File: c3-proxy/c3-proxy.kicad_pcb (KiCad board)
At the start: 4 copper layers, 69.8 x 50 mm, 73 parts, among them J1 TFM-120-X1-XXX-D-RA, J2 SFM-120-02-L-DH, J3 USB_C_Receptacle_USB2.0_16P, J4 Barrel_Jack_Switch_MountingPin, J5 Conn_01x04, Q2 DMP2035UQ-7, Q5 DMP2035UQ-7, Q6 31-DMN2053UQ-13CT-ND, Q7 DMP2035UQ-7, Q8 DMP2035UQ-7, SW1 C&K PCM13SMTR, SW2 SW_DP3T, U1 MCP2221AxST, U2 INA226, U3 LTC4412xS6, U4 LTC4412xS6, U5 TS5A21366, U6 MAX892LEUA+T, U7 MIC23050-SYML, U8 LTC4412xS6, U9 IP4234CZ6,125

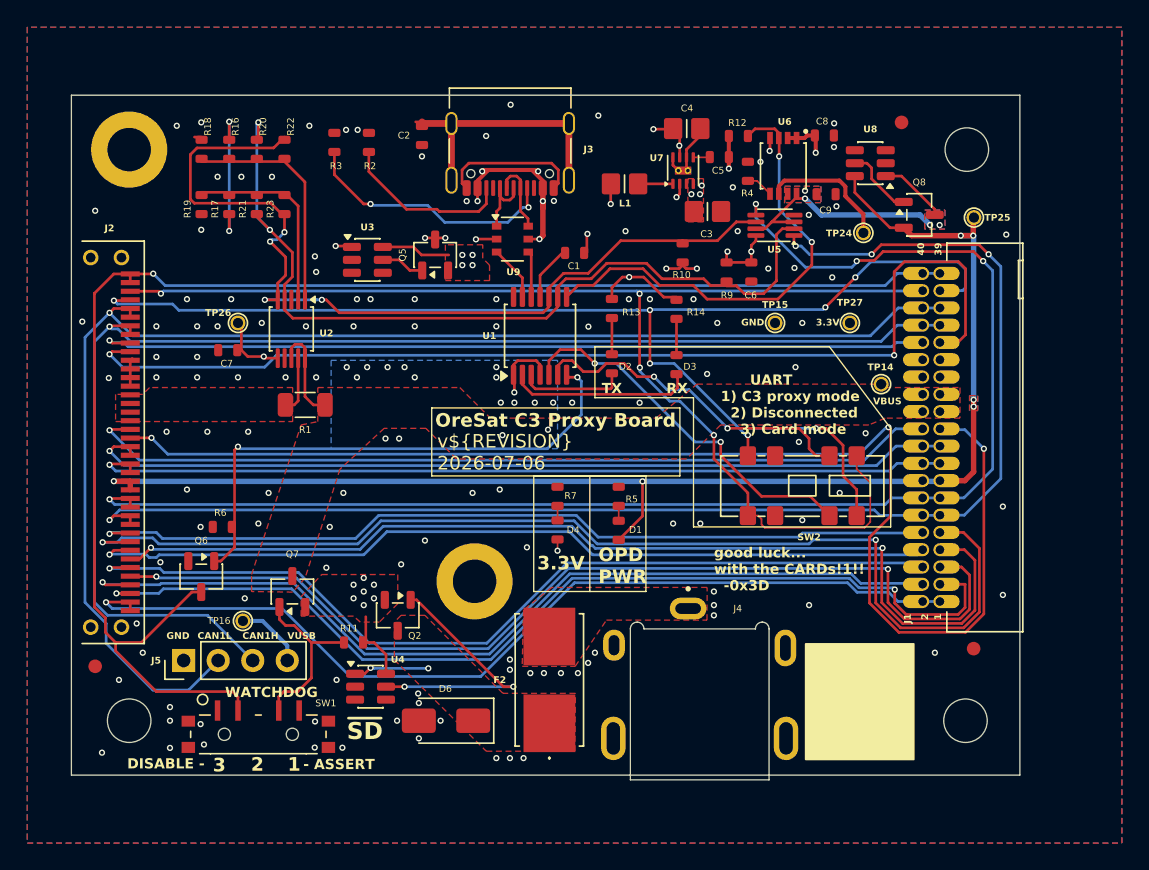
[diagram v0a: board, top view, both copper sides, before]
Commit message: changed footprints in schematic
so that "update from schematic" doesn't kill my baby resistors
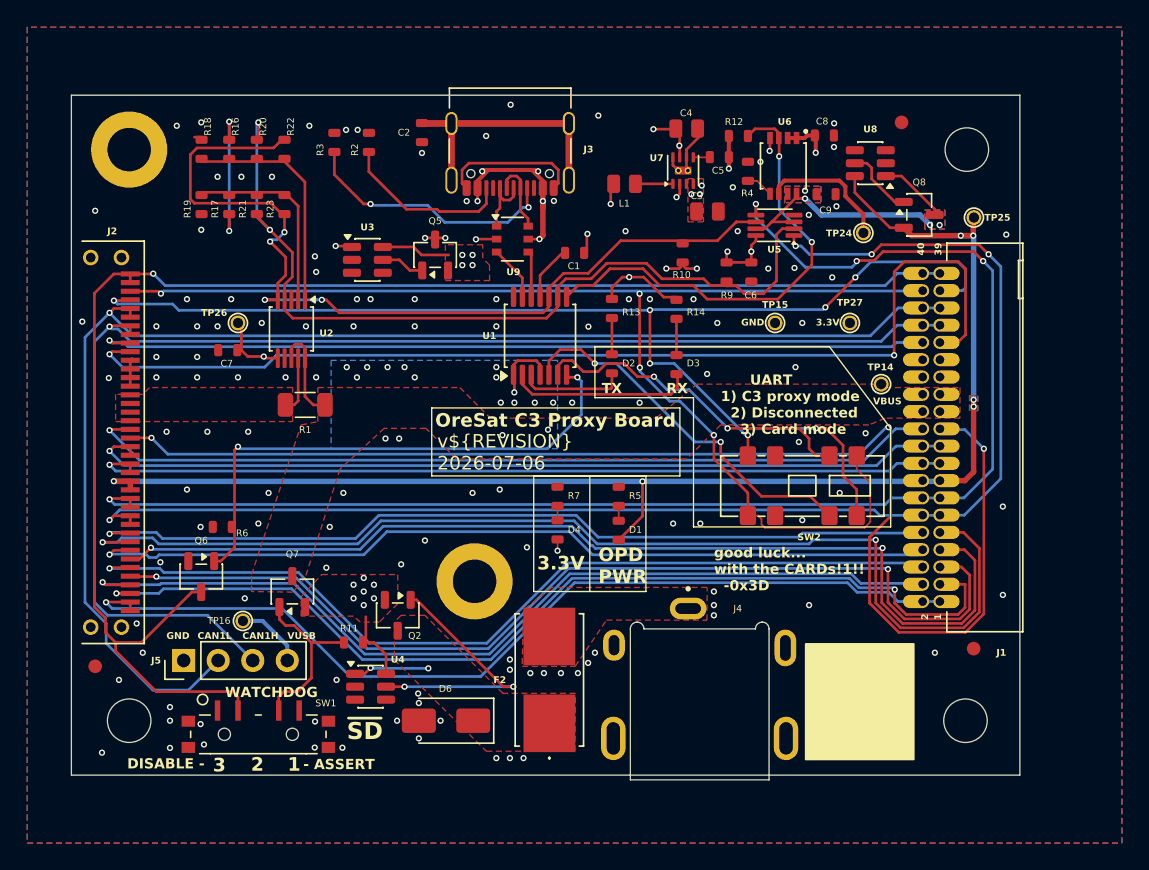
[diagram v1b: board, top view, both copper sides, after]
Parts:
- C3, C4, L1: footprint oresat-passives:0805-A -> oresat-passives:0805-C-NOSILK
- moved C2 0.21 mm to (129.0, 92.8)
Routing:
- net Net-(J3-SHIELD): track 22.0 -> 19.1 mm

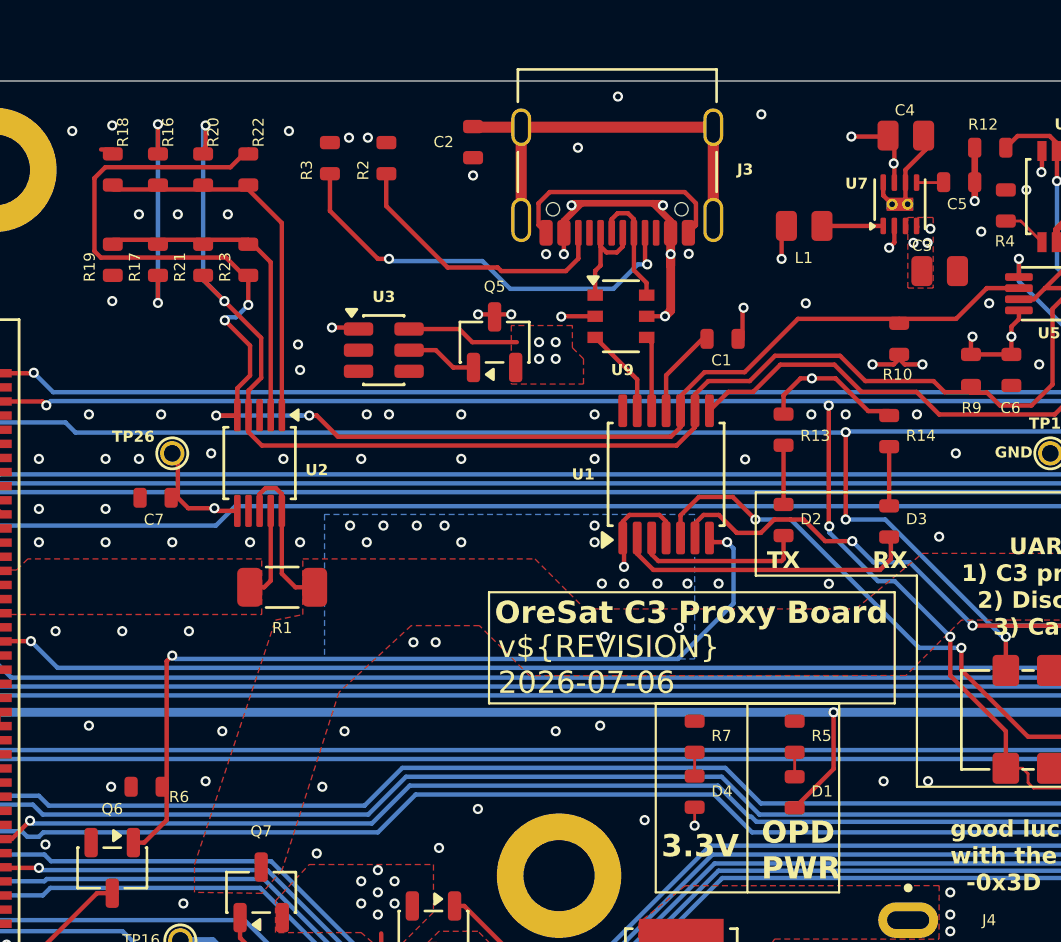
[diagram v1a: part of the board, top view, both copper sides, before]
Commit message: fixed BOM, silk art scale
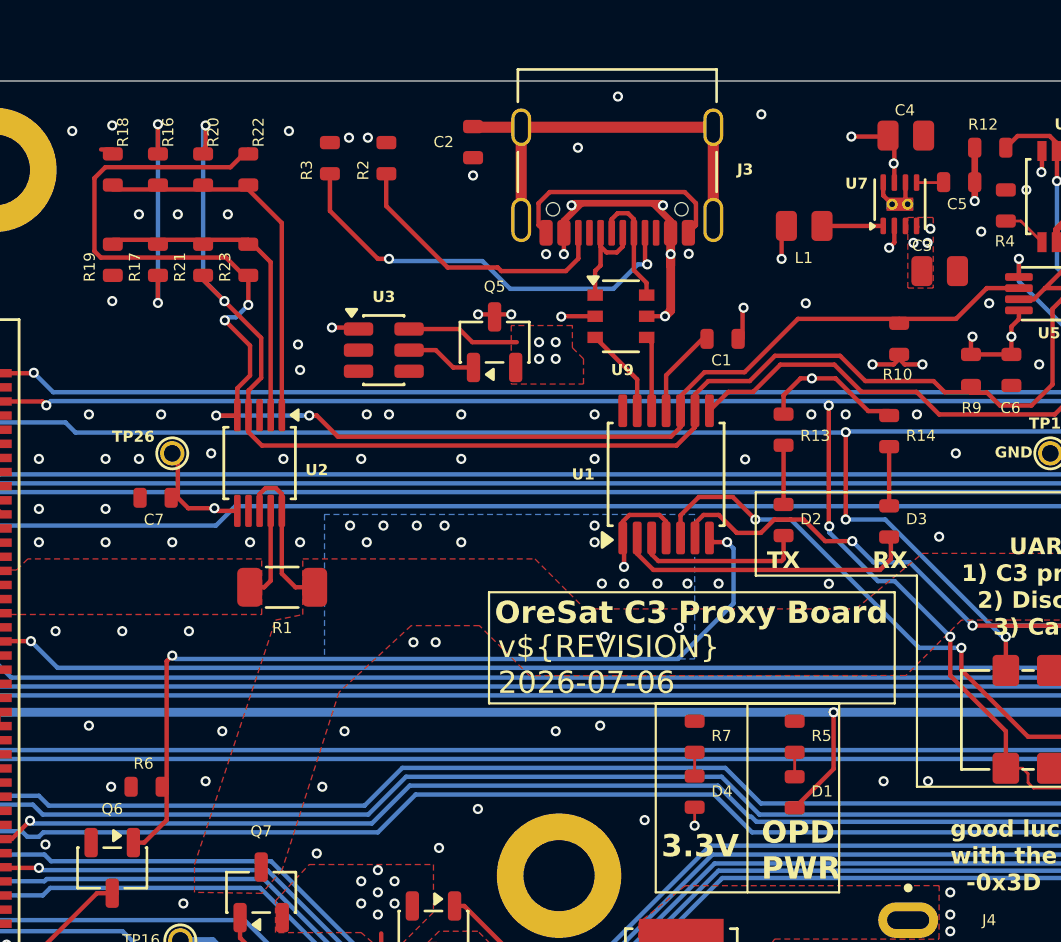
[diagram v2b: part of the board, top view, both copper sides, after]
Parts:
- moved G*** 6.53 mm to (138.8, 114.0)
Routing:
- net GND: track 21.9 -> 19.4 mm

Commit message: layout cleanup, add bypass to U1-Vdd
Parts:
- added C10: 100n, oresat-passives:0603-C-NOSILK, F.Cu at (135.1, 112.2)
- D1, D2, D3, D4: footprint oresat-passives:0603-C-NOSILK -> LED_SMD:LED_0603_1608Metric
- moved C1 2.44 mm to (138.0, 102.6), turned to -90 degrees
- moved C9 1.17 mm to (158.1, 96.3), turned to 90 degrees
- moved R5 0.28 mm to (143.5, 119.2)
- moved R7 0.25 mm to (139.0, 119.2)
- moved D2 0.09 mm to (143.0, 109.8)
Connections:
- J1 pad 2: /SPARE1 -> /SPARE2
- J2 pad 2: /SPARE1 -> /SPARE2
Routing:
- net /SPARE2: track 0.00 -> 67.3 mm, vias 0 -> 1
- net /SPARE1: track 70.0 -> 67.0 mm
- net Net-(U1-VUSB): track 3.91 -> 1.63 mm
- net 3.3V: track 41.9 -> 40.6 mm, vias 28 -> 27
- net /OPD_PWR: track 102.2 -> 102.9 mm
- net Net-(D6-K): track 5.58 -> 4.97 mm
- net GND: track 19.4 -> 19.0 mm, vias 129 -> 131

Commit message: flipped DC-jack to save clearance on the backside
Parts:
- J4: moved to B.Cu
- moved J4 1.09 mm to (149.7, 137.3), turned to 180 degrees
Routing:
- net GND: vias 131 -> 130
